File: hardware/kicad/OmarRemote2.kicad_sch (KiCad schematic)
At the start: 12 parts, among them J2 Conn_01x03, SW1 SW_Push, SW2 SW_Push, SW3 SW_Push, SW4 SW_Push, SW5 SW_Push, SW6 SW_Push, SW7 SW_DIP_x01, U1 XIAO-ESP32-S3-SMD

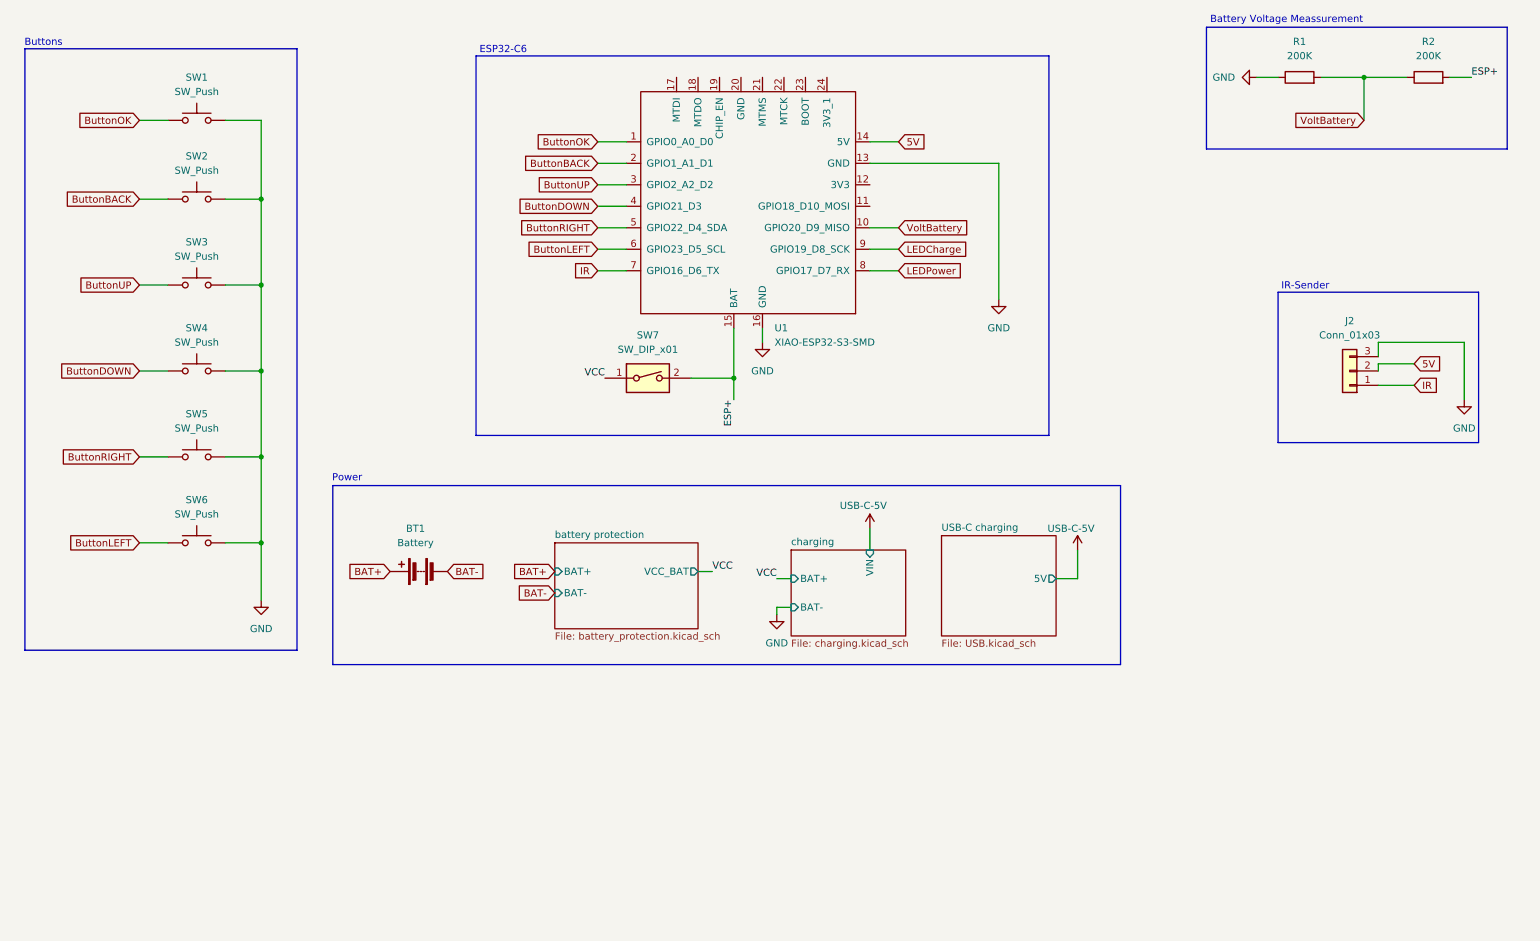
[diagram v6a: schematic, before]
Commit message: update sch to exclude IR
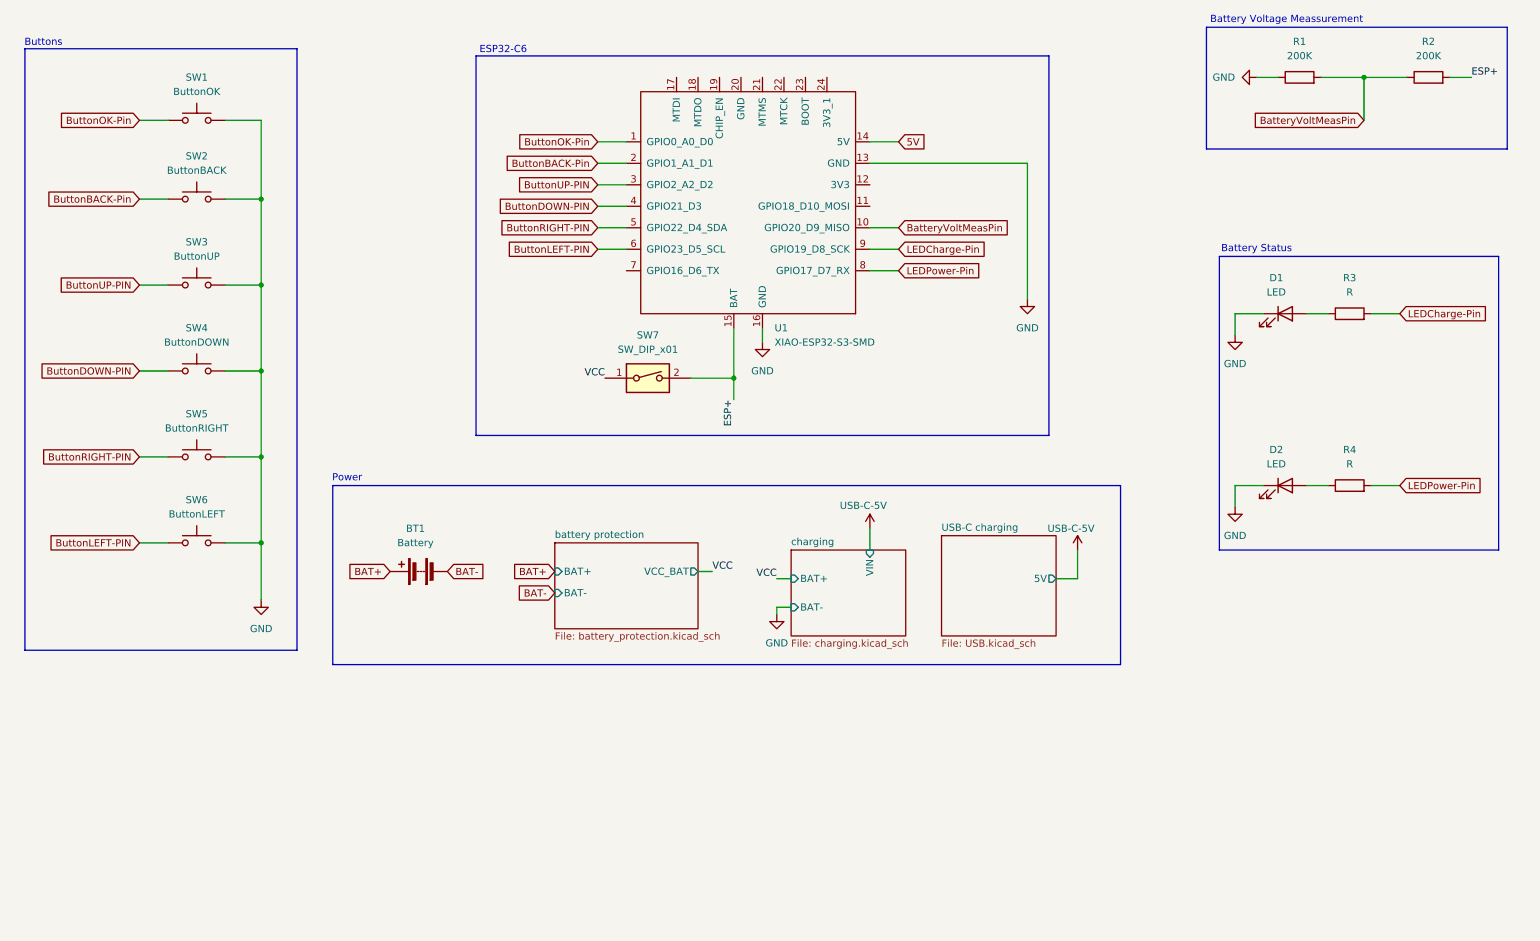
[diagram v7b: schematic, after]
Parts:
- removed J2: Conn_01x03, Connector_JST:JST_XH_B3B-XH-A_1x03_P2.50mm_Vertical, symbol Connector_Generic:Conn_01x03
- added D1, D2: LED, Connector_JST:JST_XH_B2B-XH-A_1x02_P2.50mm_Vertical, symbol Device:LED
- added R3, R4: R, Resistor_SMD:R_0805_2012Metric, symbol Device:R
- SW1: value SW_Push -> ButtonOK
- SW2: value SW_Push -> ButtonBACK
- SW3: value SW_Push -> ButtonUP
- SW4: value SW_Push -> ButtonDOWN
- SW5: value SW_Push -> ButtonRIGHT
- SW6: value SW_Push -> ButtonLEFT
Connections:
- net GND: now also D1.1 (K), D2.1 (K)
- net ButtonBACK renamed ButtonBACK-Pin
- net ButtonDOWN renamed ButtonDOWN-PIN
- net ButtonLEFT renamed ButtonLEFT-PIN
- net ButtonOK renamed ButtonOK-Pin
- net ButtonRIGHT renamed ButtonRIGHT-PIN
- net ButtonUP renamed ButtonUP-PIN
- net IR: no longer names the net of U1.7 (GPIO16_D6_TX)
- net LEDCharge renamed LEDCharge-Pin
- net LEDCharge-Pin: now also R3.2
- net LEDPower renamed LEDPower-Pin
- net LEDPower-Pin: now also R4.2
- net VoltBattery renamed BatteryVoltMeasPin
- new net: D2.2 (A), R4.1
- new net: D1.2 (A), R3.1
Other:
- note added: "Battery Status"
- note removed: "IR-Sender"
